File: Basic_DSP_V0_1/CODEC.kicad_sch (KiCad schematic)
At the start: 16 parts, among them U2 CS4270

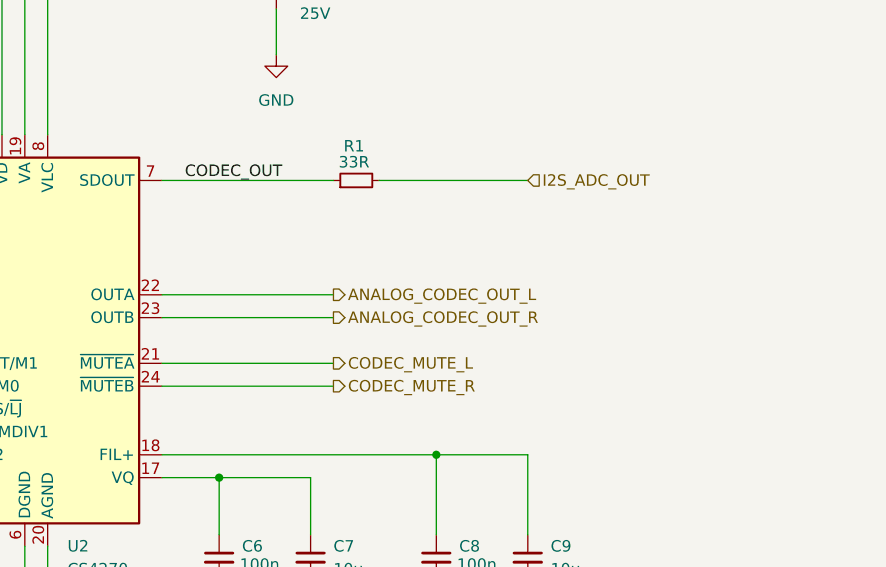
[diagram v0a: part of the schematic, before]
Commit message: Updates to basic DSP schematic
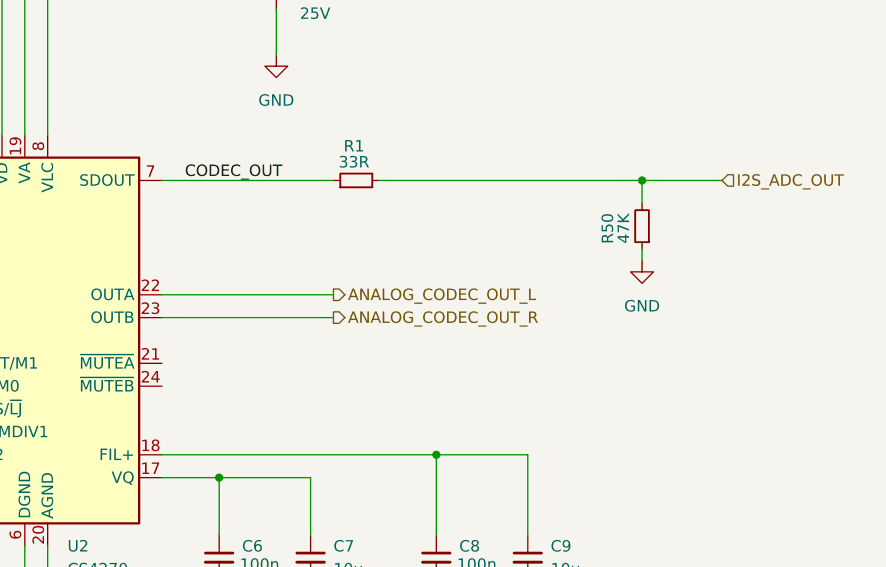
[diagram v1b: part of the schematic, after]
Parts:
- added R50: 47K, Resistor_SMD:R_0402_1005Metric_Pad0.72x0.64mm_HandSolder, symbol Device:R_Small
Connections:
- net GND: now also R50.1
- net I2S_ADC_OUT: now also R50.2
- net CODEC_MUTE_L: no longer names the net of U2.21 (~{MUTEA})
- net CODEC_MUTE_R: no longer names the net of U2.24 (~{MUTEB})
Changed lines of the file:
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@@
+	)
+	(junction
+		(at 285.75 119.38)
+		(diameter 0)
+		(color 0 0 0 0)
 	)
 	(junction
@@
 	(wire
 		(pts
+			(xy 285.75 119.38) (xy 294.64 119.38)
+		)
+		(stroke
+			(width 0)
+			(type default)
+		)
+	)
+	(wire
+		(pts
 			(xy 186.69 149.86) (xy 201.93 149.86)
 		)
@@
 	(wire
 		(pts
-			(xy 232.41 142.24) (xy 251.46 142.24)
-		)
-		(stroke
-			(width 0)
-			(type default)
-		)
-	)
-	(wire
-		(pts
 			(xy 186.69 149.86) (xy 186.69 157.48)
 		)
@@
 	(wire
 		(pts
+			(xy 285.75 119.38) (xy 285.75 121.92)
+		)
+		(stroke
+			(width 0)
+			(type default)
+		)
+	)
+	(wire
+		(pts
 			(xy 179.07 121.92) (xy 201.93 121.92)
 		)
@@
 	(wire
 		(pts
-			(xy 232.41 139.7) (xy 251.46 139.7)
-		)
-		(stroke
-			(width 0)
-			(type default)
-		)
-	)
-	(wire
-		(pts
 			(xy 245.11 92.71) (xy 245.11 95.25)
 		)
@@
 	(wire
 		(pts
+			(xy 285.75 127) (xy 285.75 128.27)
+		)
+		(stroke
+			(width 0)
+			(type default)
+		)
+	)
+	(wire
+		(pts
 			(xy 236.22 78.74) (xy 236.22 82.55)
 		)
@@
 	(wire
 		(pts
-			(xy 256.54 119.38) (xy 273.05 119.38)
+			(xy 256.54 119.38) (xy 285.75 119.38)
 		)
 		(stroke
@@
 	(hierarchical_label "I2S_ADC_OUT"
 		(shape input)
-		(at 273.05 119.38 0)
-		(fields_autoplaced yes)
-		(effects
-			(font
-				(size 1.27 1.27)
-			)
-			(justify left)
-		)
-	)
-	(hierarchical_label "CODEC_MUTE_R"
-		(shape output)
-		(at 251.46 142.24 0)
+		(at 294.64 119.38 0)
 		(fields_autoplaced yes)
 		(effects
@@
 			)
 			(justify right)
-		)
-	)
-	(hierarchical_label "CODEC_MUTE_L"
-		(shape output)
-		(at 251.46 139.7 0)
-		(fields_autoplaced yes)
-		(effects
-			(font
-				(size 1.27 1.27)
-			)
-			(justify left)
 		)
 	)
@@
 	)
 	(symbol
+		(lib_id "power:GND")
+		(at 285.75 128.27 0)
+		(unit 1)
+		(exclude_from_sim no)
+		(in_bom yes)
+		(on_board yes)
+		(dnp no)
+		(fields_autoplaced yes)
+		(property "Reference" "#PWR092"
+			(at 285.75 134.62 0)
+			(effects
+				(font
+					(size 1.27 1.27)
+				)
+				(hide yes)
+			)
+		)
+		(property "Value" "GND"
+			(at 285.75 133.35 0)
+			(effects
+				(font
+					(size 1.27 1.27)
+				)
+			)
+		)
+		(property "Footprint" ""
+			(at 285.75 128.27 0)
+			(effects
+				(font
+					(size 1.27 1.27)
+				)
+				(hide yes)
+			)
+		)
+		(property "Datasheet" ""
+			(at 285.75 128.27 0)
+			(effects
+				(font
+					(size 1.27 1.27)
+				)
+				(hide yes)
+			)
+		)
+		(property "Description" "Power symbol creates a global label with name \"GND\" , ground"
+			(at 285.75 128.27 0)
+			(effects
+				(font
+					(size 1.27 1.27)
+				)
+				(hide yes)
+			)
+		)
+		(pin "1"
+		)
+		(instances
+			(project "Basic_DSP_V0_1"
+				(path "/b632011b-bebd-450c-b21c-a571983f756a/2eb013cc-0995-4e7b-ad58-423859cd87e4"
+					(reference "#PWR092")
+					(unit 1)
+				)
+			)
+		)
+	)
+	(symbol
 		(lib_id "Device:C_Small")
 		(at 262.89 161.29 0)
@@
 					(unit 1)
 				)
+			)
+		)
+	)
+	(symbol
+		(lib_id "Device:R_Small")
+		(at 285.75 124.46 180)
+		(unit 1)
+		(exclude_from_sim no)
+		(in_bom yes)
+		(on_board yes)
+		(dnp no)
+		(property "Reference" "R50"
+			(at 281.94 124.714 90)
+			(effects
+				(font
+					(size 1.27 1.27)
+				)
+			)
+		)
+		(property "Value" "47K"
+			(at 283.718 124.714 90)
+			(effects
+				(font
+					(size 1.27 1.27)
+				)
+			)
+		)
+		(property "Footprint" "Resistor_SMD:R_0402_1005Metric_Pad0.72x0.64mm_HandSolder"
+			(at 285.75 124.46 0)
+			(effects
+				(font
+					(size 1.27 1.27)
+				)
+				(hide yes)
+			)
+		)
+		(property "Datasheet" "~"
+			(at 285.75 124.46 0)
+			(effects
+				(font
+					(size 1.27 1.27)
+				)
+				(hide yes)
+			)
+		)
+		(property "Description" "Resistor, small symbol"
+			(at 285.75 124.46 0)
+			(effects
+				(font
+					(size 1.27 1.27)
+				)
+				(hide yes)
+			)
+		)
+		(pin "2"
+		)
+		(pin "1"
+		)
+		(instances
+			(project "Basic_DSP_V0_1"
+				(path "/b632011b-bebd-450c-b21c-a571983f756a/2eb013cc-0995-4e7b-ad58-423859cd87e4"
+					(reference "R50")
+					(unit 1)
+				)

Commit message: Minor updates to Basic schematic
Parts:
- C1, C2, C3, C4, C5, C6, C8: footprint Capacitor_SMD:C_0402_1005Metric -> Capacitor_SMD:C_0603_1608Metric_Pad1.08x0.95mm_HandSolder
- C7: footprint Capacitor_SMD:C_0805_2012Metric -> Capacitor_SMD:C_0603_1608Metric_Pad1.08x0.95mm_HandSolder
- R1, R2, R3, R4, R5, R50, R6: footprint Resistor_SMD:R_0402_1005Metric_Pad0.72x0.64mm_HandSolder -> Resistor_SMD:R_0603_1608Metric_Pad0.98x0.95mm_HandSolder
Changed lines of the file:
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@@
 			)
 		)
-		(property "Footprint" "Resistor_SMD:R_0402_1005Metric_Pad0.72x0.64mm_HandSolder"
+		(property "Footprint" "Resistor_SMD:R_0603_1608Metric_Pad0.98x0.95mm_HandSolder"
 			(at 186.69 160.02 0)
 			(effects
@@
 			)
 		)
-		(property "Footprint" "Capacitor_SMD:C_0402_1005Metric"
+		(property "Footprint" "Capacitor_SMD:C_0603_1608Metric_Pad1.08x0.95mm_HandSolder"
 			(at 186.69 100.33 0)
 			(effects
@@
 			)
 		)
-		(property "Footprint" "Resistor_SMD:R_0402_1005Metric_Pad0.72x0.64mm_HandSolder"
+		(property "Footprint" "Resistor_SMD:R_0603_1608Metric_Pad0.98x0.95mm_HandSolder"
 			(at 193.04 160.02 0)
 			(effects
@@
 			)
 		)
-		(property "Footprint" "Capacitor_SMD:C_0402_1005Metric"
+		(property "Footprint" "Capacitor_SMD:C_0603_1608Metric_Pad1.08x0.95mm_HandSolder"
 			(at 245.11 97.79 0)
 			(effects
@@
 			)
 		)
-		(property "Footprint" "Capacitor_SMD:C_0805_2012Metric"
+		(property "Footprint" "Capacitor_SMD:C_0603_1608Metric_Pad1.08x0.95mm_HandSolder"
 			(at 248.92 161.29 0)
 			(effects
@@
 			)
 		)
-		(property "Footprint" "Capacitor_SMD:C_0402_1005Metric"
+		(property "Footprint" "Capacitor_SMD:C_0603_1608Metric_Pad1.08x0.95mm_HandSolder"
 			(at 262.89 161.29 0)
 			(effects
@@
 			)
 		)
-		(property "Footprint" "Capacitor_SMD:C_0402_1005Metric"
+		(property "Footprint" "Capacitor_SMD:C_0603_1608Metric_Pad1.08x0.95mm_HandSolder"
 			(at 198.12 100.33 0)
 			(effects
@@
 			)
 		)
-		(property "Footprint" "Resistor_SMD:R_0402_1005Metric_Pad0.72x0.64mm_HandSolder"
+		(property "Footprint" "Resistor_SMD:R_0603_1608Metric_Pad0.98x0.95mm_HandSolder"
 			(at 254 119.38 0)
 			(effects
@@
 			)
 		)
-		(property "Footprint" "Capacitor_SMD:C_0402_1005Metric"
+		(property "Footprint" "Capacitor_SMD:C_0603_1608Metric_Pad1.08x0.95mm_HandSolder"
 			(at 236.22 76.2 0)
 			(effects
@@
 			)
 		)
-		(property "Footprint" "Resistor_SMD:R_0402_1005Metric_Pad0.72x0.64mm_HandSolder"
+		(property "Footprint" "Resistor_SMD:R_0603_1608Metric_Pad0.98x0.95mm_HandSolder"
 			(at 199.39 160.02 0)
 			(effects
@@
 			)
 		)
-		(property "Footprint" "Resistor_SMD:R_0402_1005Metric_Pad0.72x0.64mm_HandSolder"
+		(property "Footprint" "Resistor_SMD:R_0603_1608Metric_Pad0.98x0.95mm_HandSolder"
 			(at 140.97 129.54 0)
 			(effects
@@
 			)
 		)
-		(property "Footprint" "Resistor_SMD:R_0402_1005Metric_Pad0.72x0.64mm_HandSolder"
+		(property "Footprint" "Resistor_SMD:R_0603_1608Metric_Pad0.98x0.95mm_HandSolder"
 			(at 133.35 129.54 0)
 			(effects
@@
 			)
 		)
-		(property "Footprint" "Capacitor_SMD:C_0402_1005Metric"
+		(property "Footprint" "Capacitor_SMD:C_0603_1608Metric_Pad1.08x0.95mm_HandSolder"
 			(at 226.06 76.2 0)
 			(effects
@@
 			)
 		)
-		(property "Footprint" "Resistor_SMD:R_0402_1005Metric_Pad0.72x0.64mm_HandSolder"
+		(property "Footprint" "Resistor_SMD:R_0603_1608Metric_Pad0.98x0.95mm_HandSolder"
 			(at 285.75 124.46 0)
 			(effects
@@
 			)
 		)
-		(property "Footprint" "Capacitor_SMD:C_0402_1005Metric"
+		(property "Footprint" "Capacitor_SMD:C_0603_1608Metric_Pad1.08x0.95mm_HandSolder"
 			(at 238.76 161.29 0)
 			(effects

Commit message: Updated parts with LCSC order codes
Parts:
- C1, C3, C5, C6, C8: MF TAIYO YUDEN -> FH (Guangdong Fenghua Advanced Tech); MPN MBAST105SB7104KFNA01 -> 0603B104M250NT; OC_LCSC (none) -> C336628
- C2, C4: MF Murata Electronics -> FH (Guangdong Fenghua Advanced Tech); MPN GRM155Z71A225KE01D -> 0603B225K250NT; OC_LCSC (none) -> C99228; Voltage (none) -> 25V
- C7: MPN CL21B106KOQNNNG -> CL10A106MA8NRNC; OC_LCSC (none) -> C96446; Voltage (none) -> 25V
- C9: footprint Capacitor_SMD:C_0805_2012Metric -> Capacitor_SMD:C_0603_1608Metric_Pad1.08x0.95mm_HandSolder; MPN CL21B106KOQNNNG -> CL10A106MA8NRNC; OC_LCSC (none) -> C96446; Voltage (none) -> 25V
- R1: MF (none) -> Walsin Tech Corp; MPN (none) -> WR06X33R0FTL; OC_LCSC (none) -> C163909
- R2, R3: MF (none) -> UNI-ROYAL(Uniroyal Elec); MPN (none) -> 0603WAF2201T5E; OC_LCSC (none) -> C4190
- R4, R5, R6: MF (none) -> UNI-ROYAL(Uniroyal Elec); MPN (none) -> 0603WAF1002T5E; OC_LCSC (none) -> C25804
- R50: MF (none) -> YAGEO; MPN (none) -> RC0603FR-0747KL; OC_LCSC (none) -> C105579
- U2: MF (none) -> Cirrus Logic; MPN (none) -> CS4270-CZZR; OC_LCSC (none) -> C1323229

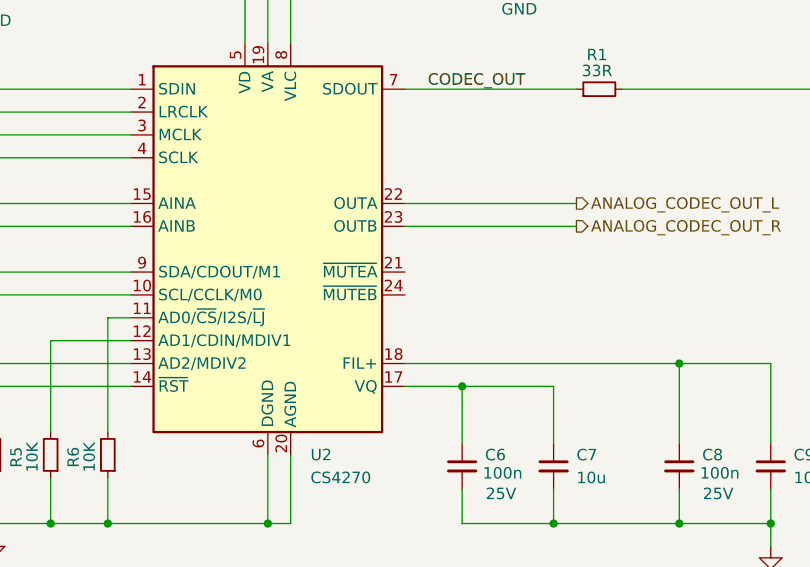
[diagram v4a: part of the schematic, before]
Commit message: Layout and removal of PDN ferrites
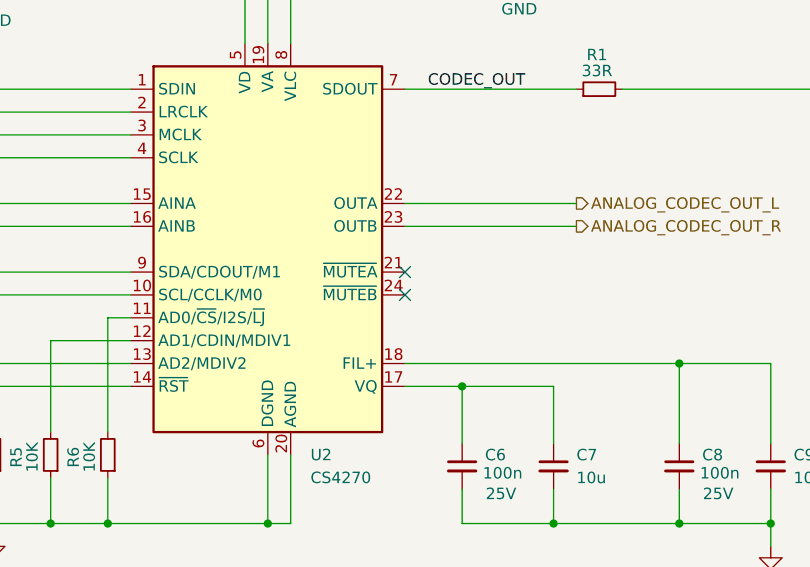
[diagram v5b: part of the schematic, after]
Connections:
- no-connect marks 0 -> 2
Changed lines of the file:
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@@
 		(color 0 0 0 0)
+	)
+	(no_connect
+		(at 232.41 139.7)
+	)
+	(no_connect
+		(at 232.41 142.24)
 	)
 	(wire
